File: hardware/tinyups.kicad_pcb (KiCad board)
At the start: 4 copper layers, 144.6 x 137.5 mm, 122 parts, among them J1 XT60, J2 XT30, J3 USB, J4 SWD, J5 FAN, Q1 N-FET 40V, Q10 N-FET 40V, Q11 N-FET 40V, Q12 N-FET 40V, Q2 N-FET 40V, Q3 N-FET 30V, Q4 N-FET 30V, Q5 N-FET 30V, Q6 N-FET 30V, Q7 N-FET 40V, Q8 N-FET 40V, Q9 N-FET 40V, U1 LM5069, U2 LM74700-Q1, U3 BQ25720, U4 LM5176, U5 BQ76942, U6 RP2040, U7 W25Q128, U8 3V3, Y1 12MHz

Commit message: more work on routing
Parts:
- moved C14 31.8 mm to (4.72, 124.5)
- moved C15 31.8 mm to (10.7, 124.5)
- moved C24 28.3 mm to (112.6, 108.4)
- moved C27 28.3 mm to (137.3, 94.5)
- moved C25 17.9 mm to (118.6, 108.4)
- moved C28 17.9 mm to (100.7, 108.4)
- moved C6 11.9 mm to (139.0, 37.9)
- moved C8 11.9 mm to (127.1, 37.9)
- moved C10 11.9 mm to (22.9, 116.9)
- moved C11 11.9 mm to (29.4, 116.9)
- moved C12 11.9 mm to (35.6, 116.9)
- moved C13 11.9 mm to (41.5, 116.9)
- moved C5 11.9 mm to (133.0, 37.9)
- moved C7 11.9 mm to (121.1, 37.9)
- moved C16 9.62 mm to (10.7, 116.9)
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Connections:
- C10 pad 2: /SW1 -> /SW1_OUT
- C11 pad 2: /SW2 -> /SW2_OUT
- L3 pad 1: /SW1 -> /SW1_OUT
- L3 pad 2: /SW2 -> /SW2_OUT
- Q10 pad 2: /SW2 -> /SW2_OUT
- Q7 pad 2: /SW1 -> /SW1_OUT
- Q8 pad 3: /SW1 -> /SW1_OUT
- Q9 pad 3: /SW2 -> /SW2_OUT
- U4 pad 15: /SW2 -> /SW2_OUT
- U4 pad 25: /SW1 -> /SW1_OUT
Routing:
- net /VIN_SYS: track 20.4 -> 304.9 mm, vias 10 -> 7
- net /SW1: track 281.0 -> 68.9 mm, vias 3 -> 5
- net /SW2: track 264.4 -> 76.2 mm, vias 9 -> 5
- net /SW2_OUT: track 0.00 -> 84.0 mm, vias 0 -> 5
- net /SW1_OUT: track 0.00 -> 71.3 mm, vias 0 -> 4
- net /ILIM_HIZ: track 41.1 -> 0.00 mm, vias 2 -> 0
- net /+3V3: track 274.9 -> 311.9 mm, vias 10 -> 8
- net /N_PGOOD: track 1.25 -> 33.0 mm, vias 1 -> 2
- net /GND: track 209.7 -> 185.2 mm, vias 41 -> 45
- net /N_SLOPE: track 14.8 -> 36.0 mm
- net /N_BOOT1: track 37.1 -> 21.5 mm
- net /VBAT: track 234.6 -> 219.4 mm, vias 9 -> 8
- net /N_DITH: track 18.5 -> 33.6 mm
- net /CELL0: track 56.0 -> 44.2 mm, vias 3 -> 4
- net /N_LED3: track 31.0 -> 42.7 mm
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- removed copper zone on In2.Cu, net /VIN_SYS

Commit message: work on routing. llm hit wall
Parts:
- moved J4 29.0 mm to (153.9, 97.2)
- moved U7 29.0 mm to (134.8, 116.3)
- moved U8 29.0 mm to (151.9, 115.3)
- moved C5 29.0 mm to (153.9, 58.0)
- moved Q6 29.0 mm to (139.1, 47.6)
- moved Cf0 29.0 mm to (73.9, 115.3)
- moved Cf1 29.0 mm to (80.4, 115.3)
- moved Cf2 29.0 mm to (86.9, 115.3)
- moved Cf4 29.0 mm to (99.9, 115.3)
- moved D3 29.0 mm to (151.4, 128.4)
- moved J2 29.0 mm to (50.3, 95.5)
- moved J3 29.0 mm to (139.8, 97.2)
- moved R18 29.0 mm to (63.6, 124.7)
- moved R33 29.0 mm to (139.4, 135.9)
- moved R35 29.0 mm to (151.2, 135.9)
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
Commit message: note amp issue
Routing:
- net /ILIM_HIZ: track 0.00 -> 43.8 mm
- net /GND: track 185.2 -> 207.7 mm, vias 45 -> 48
- net /N_COMP2: vias 1 -> 0
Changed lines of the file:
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@@
 	)
 	(segment
+		(start 123.018885 126)
+		(end 123.476401 125.542484)
+		(width 0.127)
+		(layer "F.Cu")
+		(net 2)
+	)
+	(segment
 		(start 120.677499 136.4653)
 		(end 120.677499 135.9367)
@@
 	)
 	(segment
+		(start 122.564999 128.4102)
+		(end 122.564999 126.435001)
+		(width 0.127)
+		(layer "F.Cu")
+		(net 2)
+	)
+	(segment
 		(start 148.934999 57.9712)
 		(end 148.016499 58.8897)
@@
 	)
 	(segment
+		(start 146.6358 46.7038)
+		(end 146.5 46.8396)
+		(width 0.127)
+		(layer "F.Cu")
+		(net 2)
+	)
+	(segment
 		(start 142.493199 128.4102)
 		(end 144.447499 128.4102)
@@
 	)
 	(segment
+		(start 147.934499 46.7038)
+		(end 146.6358 46.7038)
+		(width 0.127)
+		(layer "F.Cu")
+		(net 2)
+	)
+	(segment
 		(start 62.448699 137.9068)
 		(end 63.388799 136.9667)
@@
 	)
 	(segment
-		(start 147.934499 46.7038)
-		(end 147.934499 46.8396)
-		(width 0.127)
-		(layer "F.Cu")
-		(net 2)
-	)
-	(segment
 		(start 31.424999 45.8856)
 		(end 29.796599 45.8856)
@@
 	)
 	(segment
+		(start 120.677499 135.322501)
+		(end 121.5 134.5)
+		(width 0.127)
+		(layer "F.Cu")
+		(net 2)
+	)
+	(segment
 		(start 32.557499 112.6937)
 		(end 30.872699 111.0089)
@@
 	)
 	(segment
+		(start 123 126)
+		(end 123.018885 126)
+		(width 0.127)
+		(layer "F.Cu")
+		(net 2)
+	)
+	(segment
 		(start 148.016499 58.8897)
 		(end 143.905099 58.8897)
@@
 	)
 	(segment
+		(start 120.677499 135.9367)
+		(end 120.677499 135.322501)
+		(width 0.127)
+		(layer "F.Cu")
+		(net 2)
+	)
+	(segment
 		(start 62.642199 145.4185)
 		(end 63.567499 144.4932)
@@
 	)
 	(segment
+		(start 52.258499 126.5902)
+		(end 52.429999 126.7617)
+		(width 0.127)
+		(layer "F.Cu")
+		(net 2)
+	)
+	(segment
 		(start 56.133499 124.9902)
 		(end 56.974999 124.9902)
@@
 	)
 	(segment
+		(start 54.595999 127.007998)
+		(end 54.595999 128.1735)
+		(width 0.127)
+		(layer "F.Cu")
+		(net 2)
+	)
+	(segment
 		(start 133.777099 66.4588)
 		(end 134.745999 67.4277)
@@
 	)
 	(segment
+		(start 52.429999 126.7617)
+		(end 54.349701 126.7617)
+		(width 0.127)
+		(layer "F.Cu")
+		(net 2)
+	)
+	(segment
 		(start 101.220799 106.8483)
 		(end 101.650399 106.8483)
@@
 	)
 	(segment
+		(start 54.349701 126.7617)
+		(end 54.595999 127.007998)
+		(width 0.127)
+		(layer "F.Cu")
+		(net 2)
+	)
+	(segment
 		(start 124.232499 117.7037)
 		(end 124.232499 119.4959)
@@
 	)
 	(segment
+		(start 122.564999 126.435001)
+		(end 123 126)
+		(width 0.127)
+		(layer "F.Cu")
+		(net 2)
+	)
+	(segment
 		(start 124.787199 68.4023)
 		(end 127.540399 68.4023)
@@
 	)
 	(via
-		(at 147.934499 46.8396)
-		(size 0.6)
-		(drill 0.3)
-		(layers "F.Cu" "B.Cu")
-		(net 2)
-	)
-	(via
-		(at 54.595999 128.1735)
+		(at 146.5 46.8396)
 		(size 0.6)
 		(drill 0.3)
@@
 	)
 	(via
+		(at 121.5 134.5)
+		(size 0.6)
+		(drill 0.3)
+		(layers "F.Cu" "B.Cu")
+		(net 2)
+	)
+	(via
+		(at 54.595999 128.1735)
+		(size 0.6)
+		(drill 0.3)
+		(layers "F.Cu" "B.Cu")
+		(net 2)
+	)
+	(via
 		(at 43.831799 46.1857)
 		(size 0.6)
@@
 	)
 	(via
+		(at 123 126)
+		(size 0.6)
+		(drill 0.3)
+		(layers "F.Cu" "B.Cu")
+		(net 2)
+	)
+	(via
 		(at 136.528099 113.6218)
 		(size 0.6)
@@
 	)
 	(via
+		(at 123.476401 125.542484)
+		(size 0.6)
+		(drill 0.3)
+		(layers "F.Cu" "B.Cu")
+		(net 2)
+	)
+	(via
 		(at 26.564999 145.6946)
 		(size 0.6)
@@
 	)
 	(segment
+		(start 126.119699 129.880301)
+		(end 126.119699 129.5655)
+		(width 0.127)
+		(layer "B.Cu")
+		(net 2)
+	)
+	(segment
+		(start 121.5 134.5)
+		(end 126.119699 129.880301)
+		(width 0.127)
+		(layer "B.Cu")
+		(net 2)
+	)
+	(segment
+		(start 122.714099 124.780182)
+		(end 122.714099 120.2669)
+		(width 0.127)
+		(layer "B.Cu")
+		(net 2)
+	)
+	(segment
+		(start 123.476401 125.542484)
+		(end 122.714099 124.780182)
+		(width 0.127)
+		(layer "B.Cu")
+		(net 2)
+	)
+	(segment
 		(start 84.799199 39.3256)
 		(end 84.796999 39.3256)
@@
 		(net 31)
 	)
-	(via
-		(at 127.458699 66.584)
-		(size 0.6)
-		(drill 0.3)
-		(layers "F.Cu" "B.Cu")
-		(net 31)
-	)
 	(segment
 		(start 149.184199 50.6278)
@@
 	)
 	(segment
+		(start 122.125819 66.5127)
+		(end 126.909319 66.5127)
+		(width 0.2)
+		(layer "F.Cu")
+		(net 81)
+	)
+	(segment
+		(start 148.9947 46.9947)
+		(end 149 47)
+		(width 0.2)
+		(layer "F.Cu")
+		(net 81)
+	)
+	(segment
+		(start 120.682499 74.9542)
+		(end 121.874999 73.7617)
+		(width 0.2)
+		(layer "F.Cu")
+		(net 81)
+	)
+	(segment
+		(start 121.874999 66.76352)
+		(end 122.125819 66.5127)
+		(width 0.2)
+		(layer "F.Cu")
+		(net 81)
+	)
+	(segment
+		(start 136.365819 57.0562)
+		(end 137.9438 57.0562)
+		(width 0.2)
+		(layer "F.Cu")
+		(net 81)
+	)
+	(segment
+		(start 137.9438 57.0562)
+		(end 148.0053 46.9947)
+		(width 0.2)
+		(layer "F.Cu")
+		(net 81)
+	)
+	(segment
+		(start 121.874999 73.7617)
+		(end 121.874999 66.76352)
+		(width 0.2)
+		(layer "F.Cu")
+		(net 81)
+	)
+	(segment
+		(start 126.909319 66.5127)
+		(end 136.365819 57.0562)
+		(width 0.2)
+		(layer "F.Cu")
+		(net 81)
+	)
+	(segment
+		(start 148.0053 46.9947)
+		(end 148.769799 46.9947)
+		(width 0.2)
+		(layer "F.Cu")
+		(net 81)
+	)
+	(segment

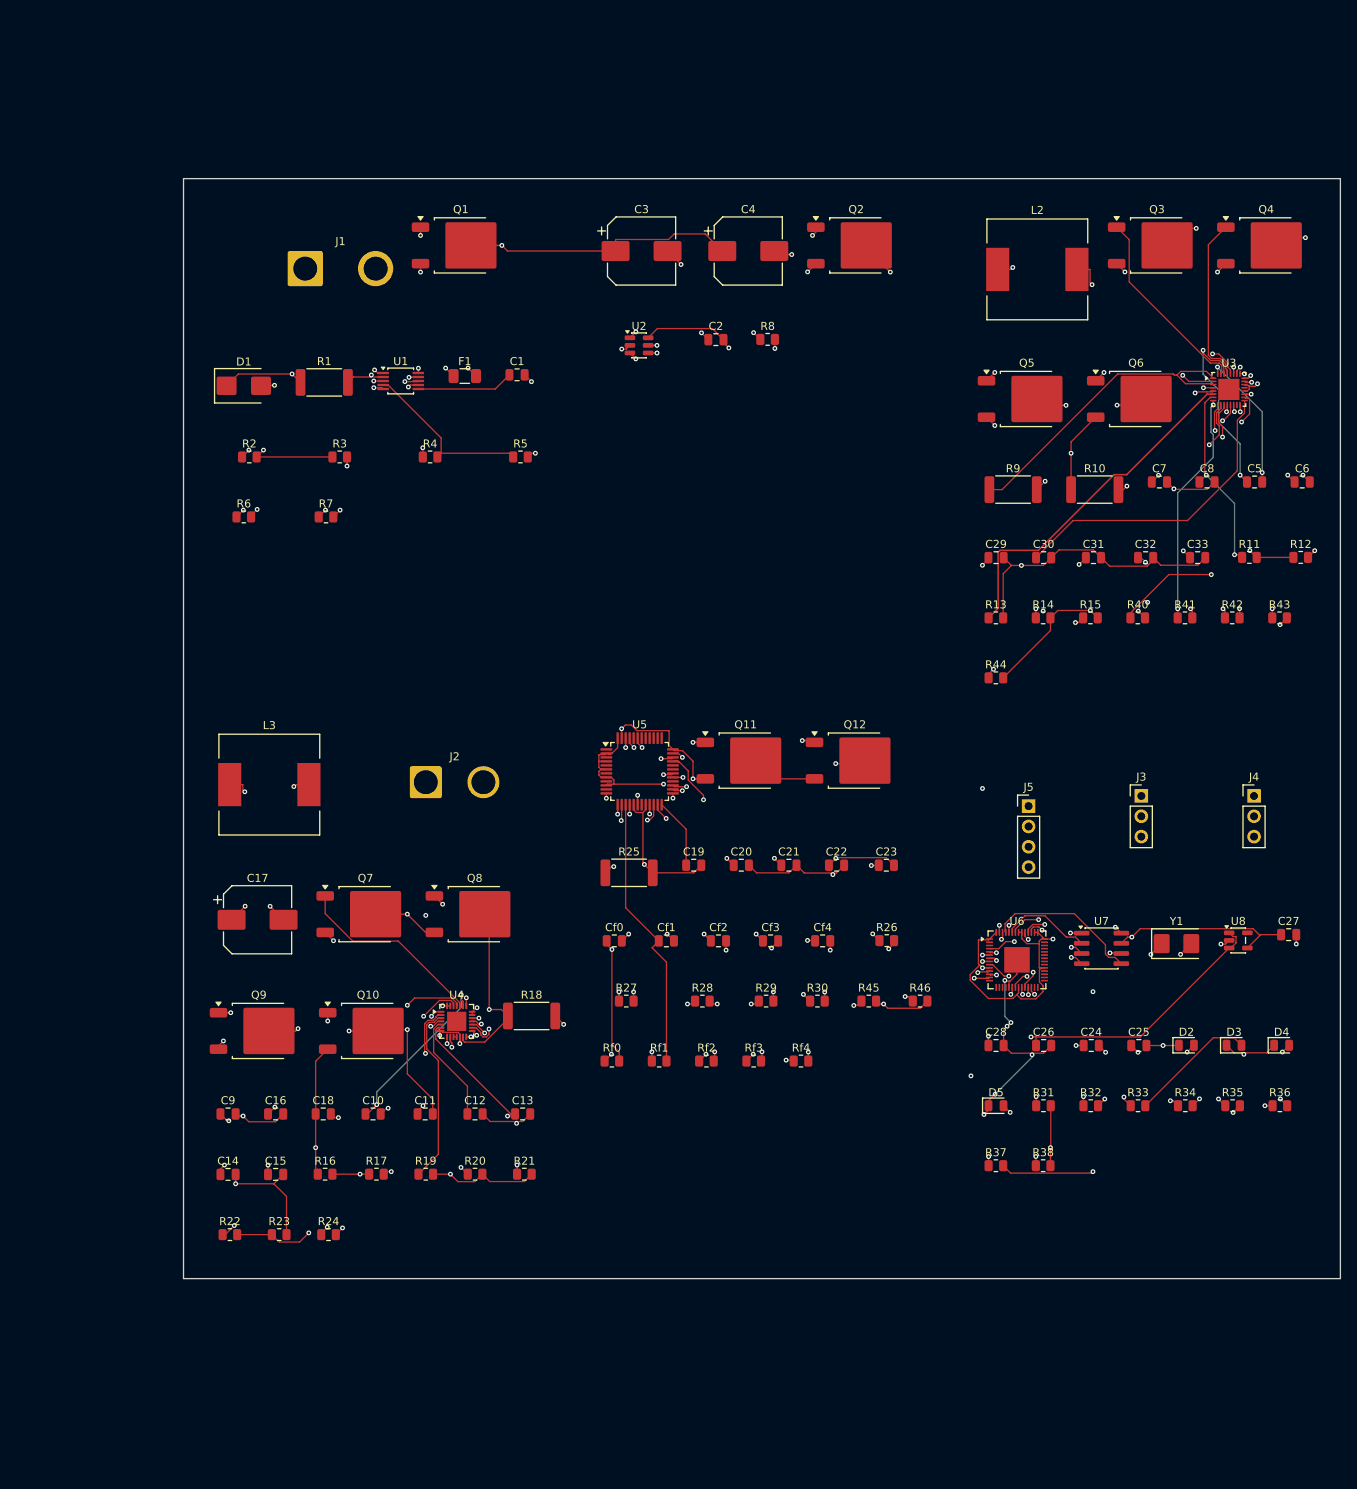
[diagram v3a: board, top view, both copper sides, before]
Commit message: quantify power components, placement, add render for inspection
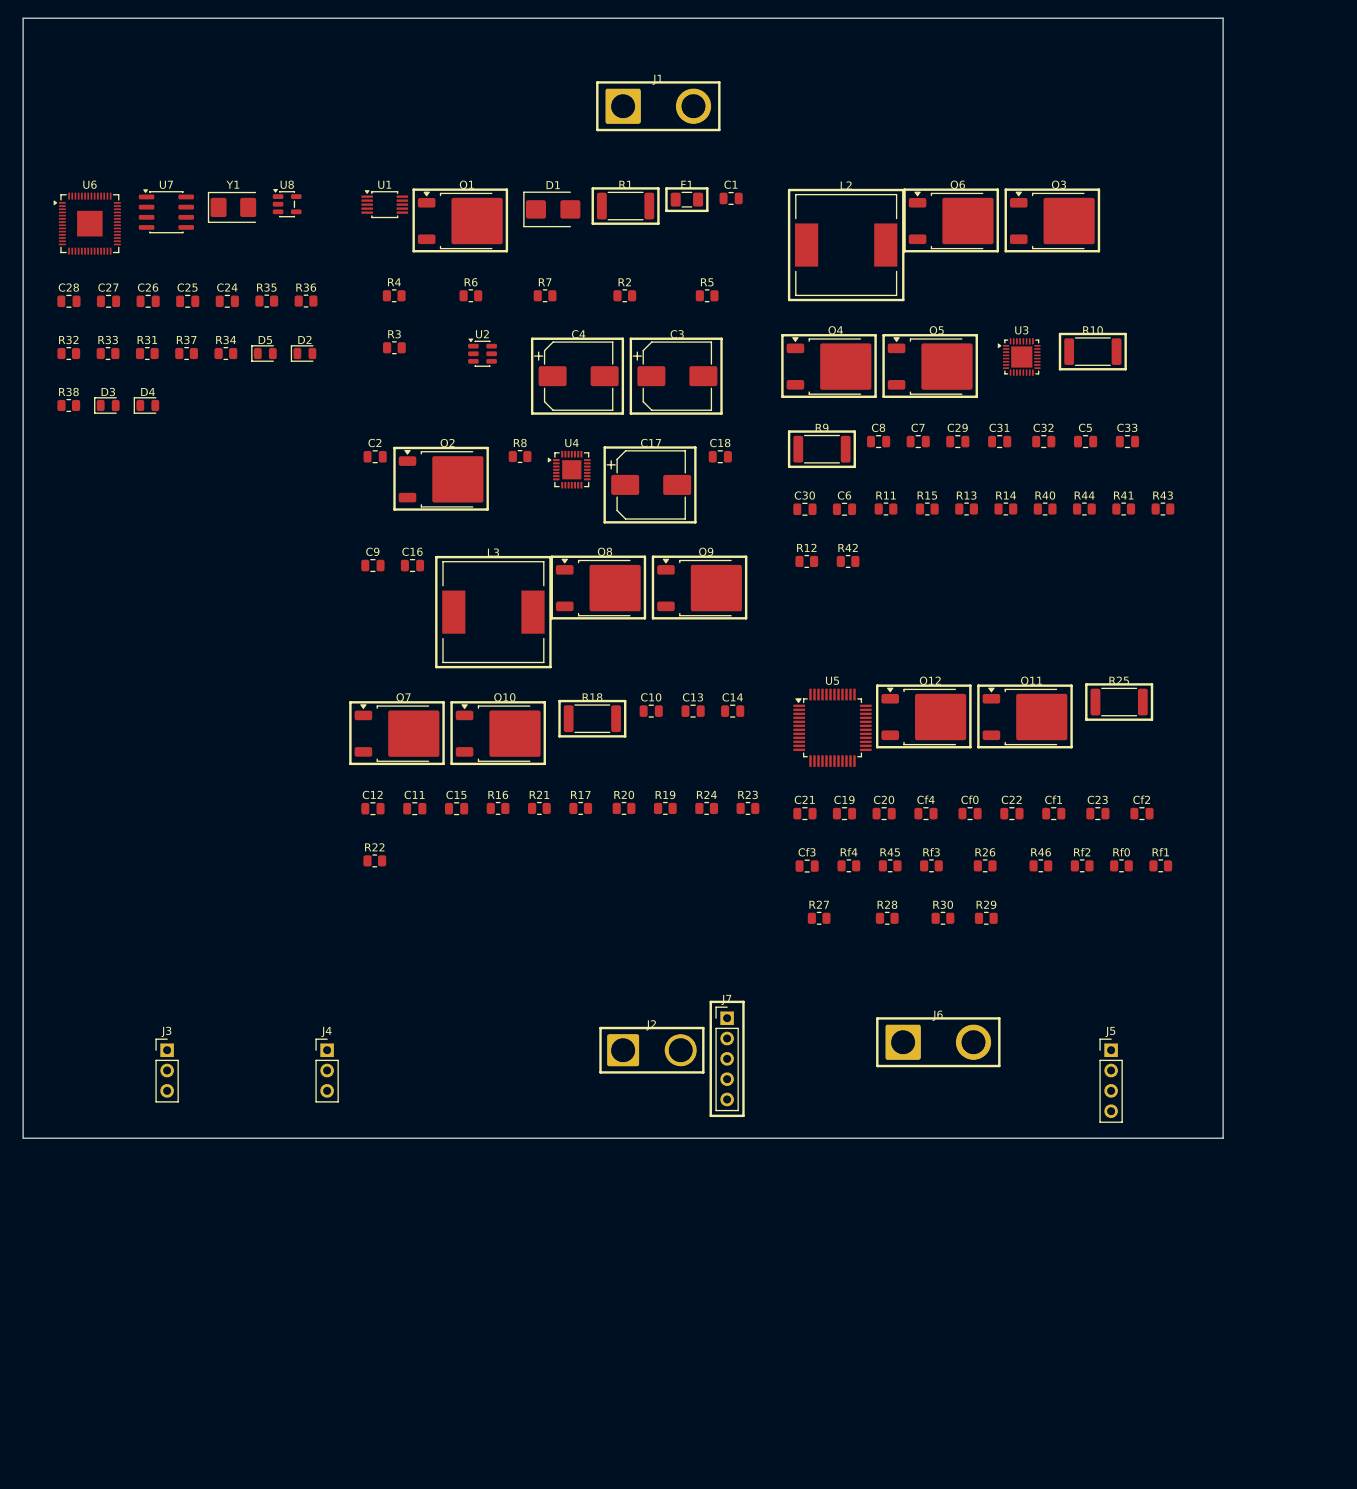
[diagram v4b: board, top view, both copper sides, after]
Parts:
- added J6: PACK, Connector_Wire:SolderWire-2.5sqmm_1x02_P8.8mm_D2.4mm_OD4.4mm, F.Cu at (110.0, 128.0)
- added J7: CELLS, Connector_PinHeader_2.54mm:PinHeader_1x05_P2.54mm_Vertical, F.Cu at (88.0, 125.0)
- moved C27 167.4 mm to (10.7, 35.4)
- moved D4 162.7 mm to (15.6, 48.4)
- moved D3 161.9 mm to (10.6, 48.4)
- moved R33 159.4 mm to (10.6, 41.9)
- moved R32 158.6 mm to (5.71, 41.9)
- moved R36 157.9 mm to (35.4, 35.4)
- moved R35 157.1 mm to (30.5, 35.4)
- moved R38 154.5 mm to (5.71, 48.4)
- moved R34 152.4 mm to (25.3, 41.9)
- moved C25 151.0 mm to (20.6, 35.4)
- moved U8 150.3 mm to (33.0, 23.2)
- moved Y1 149.6 mm to (26.3, 23.6)
- moved U7 148.8 mm to (17.9, 24.2)
- moved C28 148.6 mm to (5.72, 35.4)
- moved U6 148.0 mm to (8.34, 25.7)
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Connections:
- C22 pad 1: /VBAT -> /PACK+
- C23 pad 2: /VBAT -> /PACK+
- Q11 pad 3: /VBAT -> /PACK+
- Q12 pad 2: /VBAT -> /N_PACKMID
- Q12 pad 3: /N_PACKMID -> /VBAT
- Q2 pad 3: /N_CATH -> /VIN_SYS
- U2 pad 4: /N_CATH -> /VIN_SYS
- U5 pad 36: /VBAT -> /PACK+
- U5 pad 47: /VBAT -> /PACK+
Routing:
- net /+3V3: track 311.9 -> 0.00 mm, vias 8 -> 0
- net /VIN_SYS: track 304.9 -> 0.00 mm, vias 7 -> 0
- net /VBAT: track 219.4 -> 0.00 mm, vias 8 -> 0
- net /GND: track 207.7 -> 0.00 mm, vias 48 -> 0
- net /VOUT12: track 181.7 -> 0.00 mm, vias 4 -> 0
- net /I2C_SCL: track 133.8 -> 0.00 mm, vias 4 -> 0
- net /I2C_SDA: track 124.1 -> 0.00 mm, vias 5 -> 0
- net /IN_VALID: track 112.4 -> 0.00 mm, vias 3 -> 0
- net /SW2_OUT: track 84.0 -> 0.00 mm, vias 5 -> 0
- net /SW2: track 76.2 -> 0.00 mm, vias 5 -> 0
- net /SW1_OUT: track 71.3 -> 0.00 mm, vias 4 -> 0
- net /SW1: track 68.9 -> 0.00 mm, vias 5 -> 0
- net /CELL4: track 60.2 -> 0.00 mm, vias 2 -> 0
- net /N_USBDP_C: track 59.0 -> 0.00 mm, vias 1 -> 0
- net /VIN_LM: track 58.2 -> 0.00 mm, vias 4 -> 0
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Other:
- board size 144.6 x 137.5 mm -> 150 x 140 mm

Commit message: refine placement calculation
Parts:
- moved R38 126.1 mm to (118.5, 104.7)
- moved R32 126.0 mm to (118.5, 98.2)
- moved R33 126.0 mm to (123.4, 98.2)
- moved C23 122.3 mm to (13.5, 80.8)
- moved C33 122.2 mm to (17.1, 35.5)
- moved R35 120.4 mm to (133.2, 98.2)
- moved D2 117.3 mm to (138.1, 98.2)
- moved R36 112.2 mm to (128.3, 98.2)
- moved Cf2 112.0 mm to (29.5, 80.8)
- moved R37 108.8 mm to (113.6, 98.2)
- moved D3 108.8 mm to (103.7, 104.7)
- moved C22 106.5 mm to (18.7, 80.8)
- moved C29 106.4 mm to (11.8, 35.5)
- moved C32 106.4 mm to (22.6, 35.5)
- moved D4 105.5 mm to (108.6, 98.2)
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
